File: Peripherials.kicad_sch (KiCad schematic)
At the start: 24 parts, among them J10 IDC_Cable_02x08, J6 Conn_01x02_Pin, J7 USB_C_Receptacle_USB2.0_14P, J8 USB_C_Receptacle_USB2.0_14P, Q1 NMOS, U5 USBLC6-2P6, U6 USBLC6-2P6

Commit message: Major Changes - Schematic Done??
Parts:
- added C41: 100n, Capacitor_SMD:C_0603_1608Metric, symbol Device:C
- added J18: Micro_SD_Card, Connector_Card:microSD_HC_Hirose_DM3BT-DSF-PEJS, symbol Connector:Micro_SD_Card
- added R61, R62: DNP, Resistor_SMD:R_0603_1608Metric, symbol Device:R
- C22: renamed from C26; footprint (none) -> Capacitor_SMD:C_0603_1608Metric
- C23: renamed from C27; footprint (none) -> Capacitor_SMD:C_0603_1608Metric
- C24: renamed from C25; footprint (none) -> Capacitor_SMD:C_0603_1608Metric
- C25: renamed from C28; footprint (none) -> Capacitor_SMD:C_0603_1608Metric
- D6: renamed from D2; footprint Package_TO_SOT_SMD:SOT-666 -> Diode_SMD:D_1206_3216Metric_Pad1.42x1.75mm_HandSolder
- D7: renamed from D1; footprint Package_TO_SOT_SMD:SOT-666 -> Diode_SMD:D_1206_3216Metric_Pad1.42x1.75mm_HandSolder
- D8: renamed from D3; footprint Package_TO_SOT_SMD:SOT-666 -> Diode_SMD:D_0805_2012Metric_Pad1.15x1.40mm_HandSolder
- J12: renamed from J7; footprint (none) -> Connector_USB:USB_C_Receptacle_Palconn_UTC16-G
- J13: renamed from J8; footprint (none) -> Connector_USB:USB_C_Receptacle_Palconn_UTC16-G
- J15: renamed from J6; footprint (none) -> Connector_PinHeader_2.54mm:PinHeader_1x02_P2.54mm_Vertical
- Q2: renamed from Q1; footprint (none) -> Package_TO_SOT_SMD:SOT-23
- R44: renamed from R10; footprint Package_DIP:DIP-8_W7.62mm -> Resistor_SMD:R_0603_1608Metric
- R45: renamed from R14; footprint Package_DIP:DIP-8_W7.62mm -> Resistor_SMD:R_0603_1608Metric
- R46: renamed from R11; footprint Package_DIP:DIP-8_W7.62mm -> Resistor_SMD:R_0603_1608Metric
- R47: renamed from R15; footprint Package_DIP:DIP-8_W7.62mm -> Resistor_SMD:R_0603_1608Metric
- R48: renamed from R13; footprint Package_DIP:DIP-8_W7.62mm -> Resistor_SMD:R_0603_1608Metric
- R49: renamed from R12; footprint Package_DIP:DIP-8_W7.62mm -> Resistor_SMD:R_0603_1608Metric
- R50: renamed from R17; footprint Package_DIP:DIP-8_W7.62mm -> Resistor_SMD:R_0603_1608Metric
- R51: renamed from R16; footprint Package_DIP:DIP-8_W7.62mm -> Resistor_SMD:R_0603_1608Metric
- R52: renamed from R24; footprint Package_DIP:DIP-8_W7.62mm -> Resistor_SMD:R_0603_1608Metric
- R53: renamed from R23; footprint Package_DIP:DIP-8_W7.62mm -> Resistor_SMD:R_0603_1608Metric
- renumbered J10 to J14, U5 to U12, U6 to U13
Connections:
- net GND: now also C41.2, J18.6 (VSS), J18.SH (SHIELD), R61.1, R62.1
- net at J13.SH (SHIELD): now also R62.2
- net at J12.SH (SHIELD): now also R61.2
- net +5V renamed 5V
- net USB_D_N_ESD renamed USB_P_ESP_ESD
- net USB_P_ESP_ESD: no longer R49.2, U12.3 (I/O2)
- net USB_D_N_Resistor renamed USB_N_ESP_RES
- net USB_N_ESP_RES: no longer J12.A7 (D-), J12.B7 (D-), R48.1
- net USB_D_P_ESD renamed USB_N_ESP_ESD
- net USB_N_ESP_ESD: no longer R48.2, U12.1 (I/O1)
- net USB_D_P_Resistor renamed USB_P_ESP_RES
- net USB_P_ESP_RES: no longer J12.A6 (D+), J12.B6 (D+), R49.1
- new net 3V3: C41.1, J18.4 (VDD)
- new net SPI1_MISO: J18.7 (DAT0)
- new net SPI1_MOSI: J18.8 (DAT1)
- new net SPI1_SCLK: J18.5 (CLK)
- new net SPI_CS_SD_CARD: J18.3 (CMD)
- new net USB_N_STM_ESD: R48.2, U12.1 (I/O1)
- new net USB_N_STM_RES: J12.A7 (D-), J12.B7 (D-), R48.1
- new net USB_P_STM_ESD: R49.2, U12.3 (I/O2)
- new net USB_P_STM_RES: J12.A6 (D+), J12.B6 (D+), R49.1
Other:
- note added: "MICRO SD CARD"
- note removed: "IR EMITTER"
- moved on the sheet: C22, C23, C24, C25, D6, D7, D8, J12, J13, J14, J15, Q2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

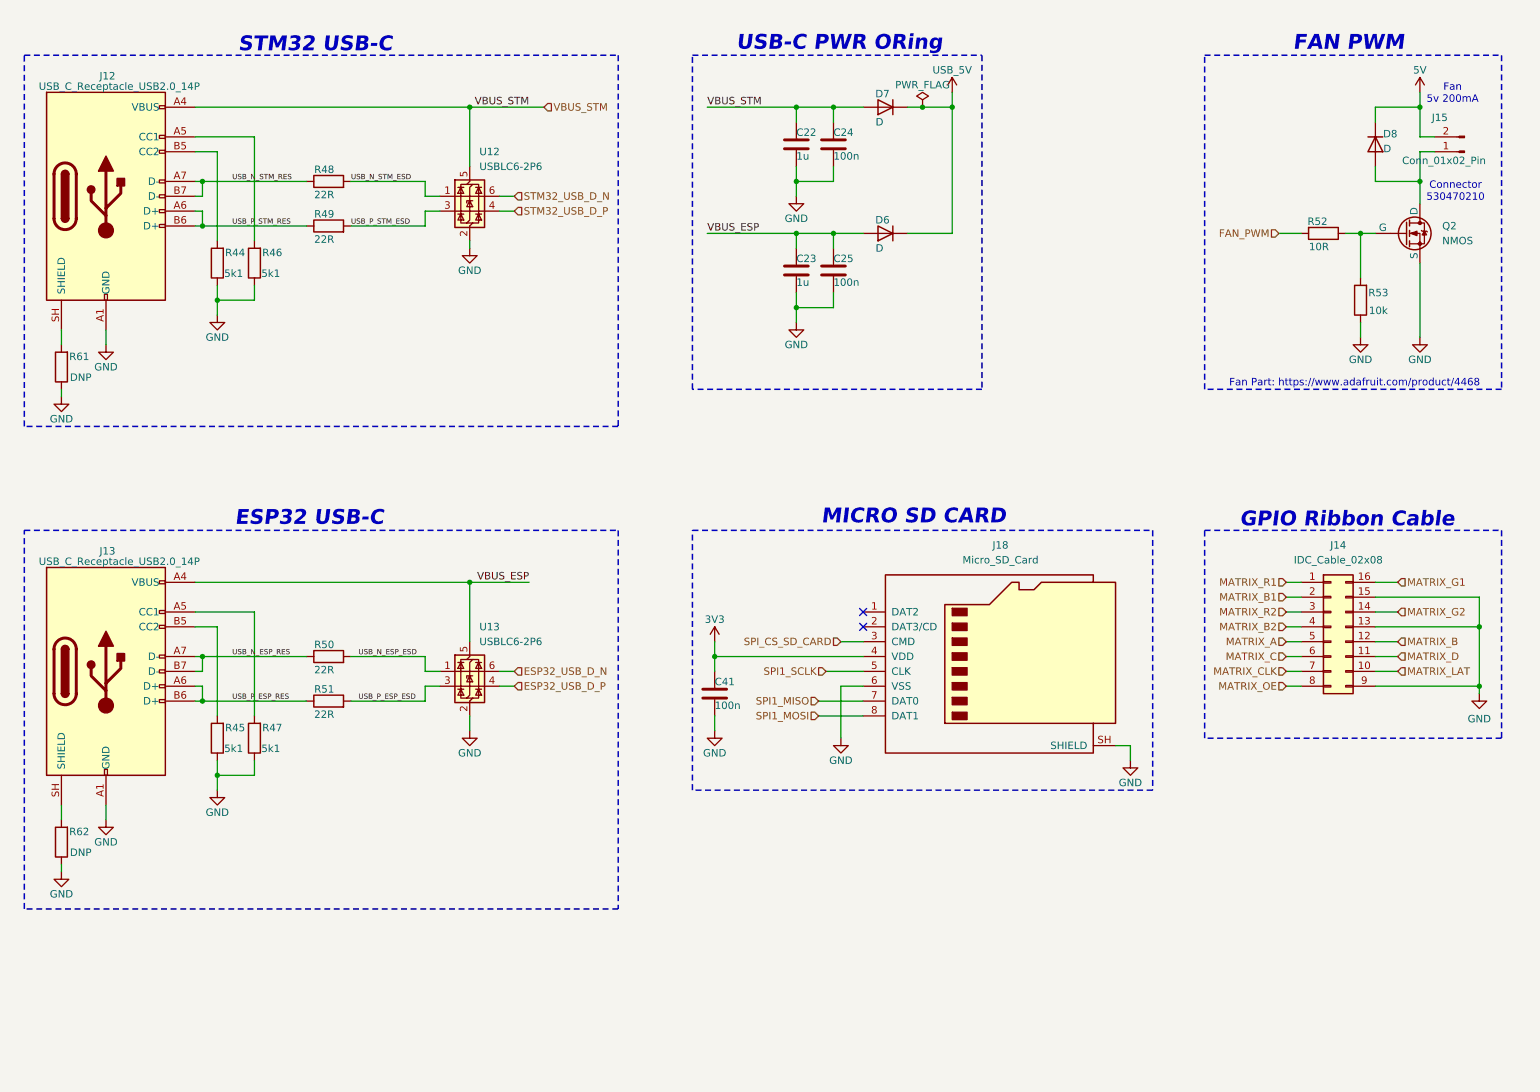
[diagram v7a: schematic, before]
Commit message: PCB Start, Schematic polish
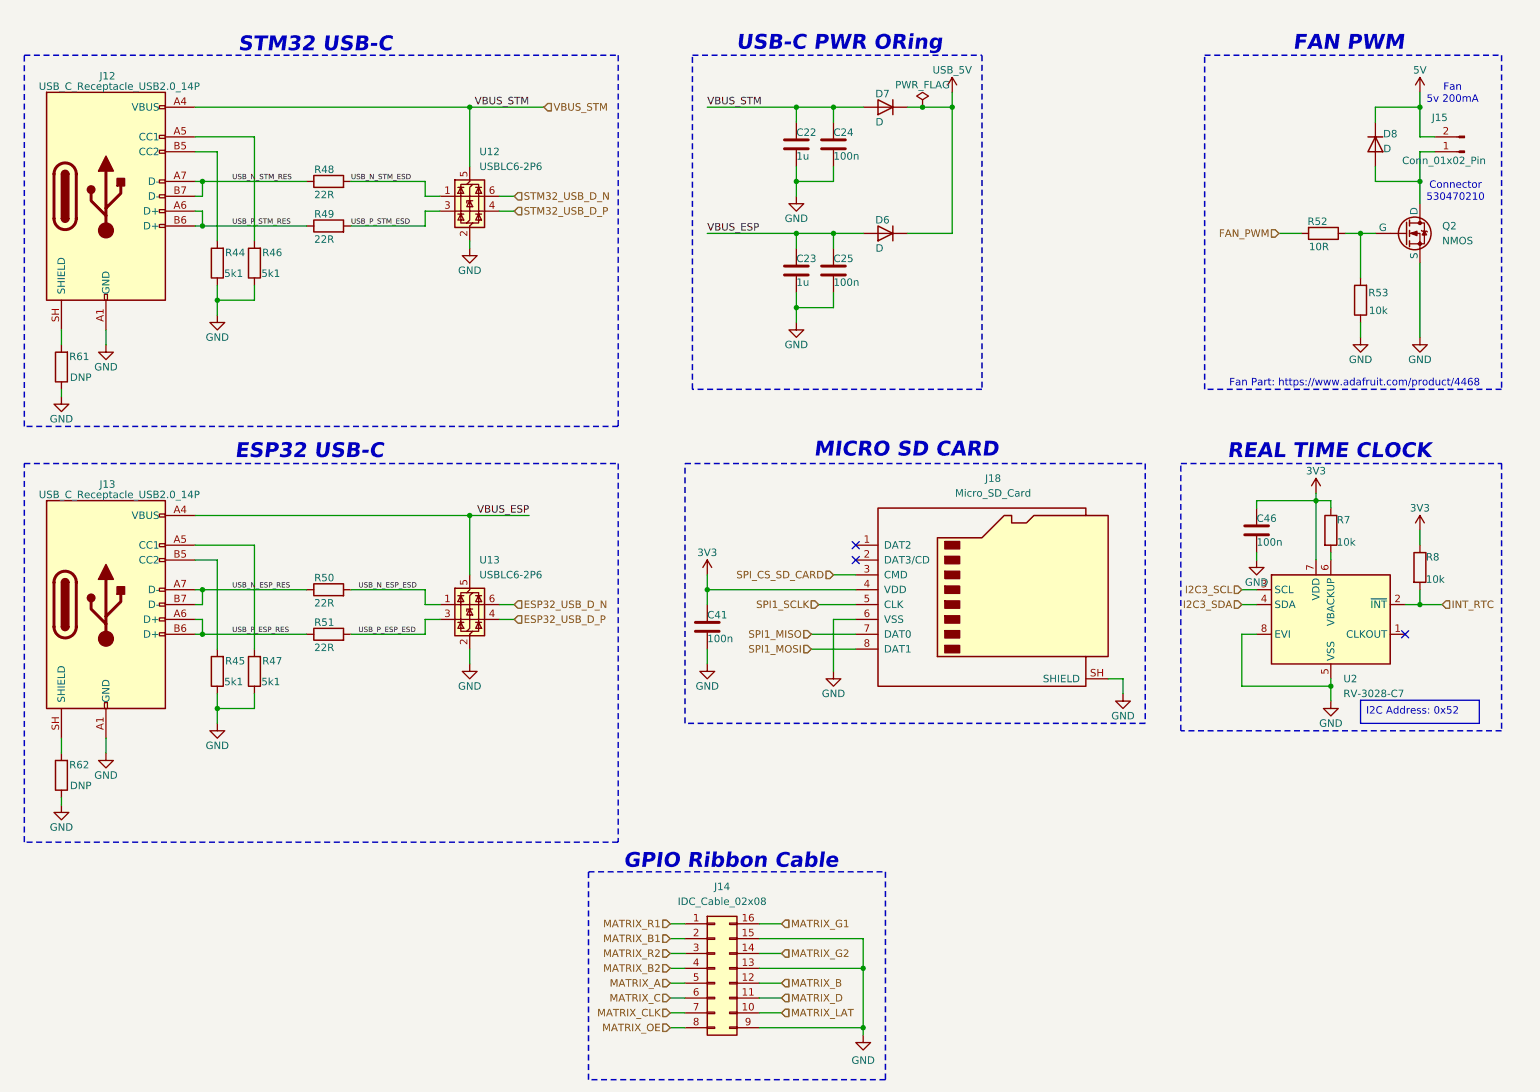
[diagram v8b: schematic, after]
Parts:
- added C46: 100n, Capacitor_SMD:C_0603_1608Metric, symbol Device:C
- added R7, R8: 10k, Resistor_SMD:R_0603_1608Metric, symbol Device:R
- added U2: RV-3028-C7, Package_SON:MicroCrystal_C7_SON-8_1.5x3.2mm_P0.9mm, symbol Timer_RTC:RV-3028-C7
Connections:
- net 3V3: now also C46.1, R7.1, R8.1, U2.7 (VDD)
- net GND: now also C46.2, U2.5 (VSS), U2.8 (EVI)
- new net: R7.2, U2.6 (VBACKUP)
- new net I2C3_SCL: U2.3 (SCL)
- new net I2C3_SDA: U2.4 (SDA)
- new net INT_RTC: R8.2, U2.2 (~{INT})
- no-connect marks 2 -> 3
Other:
- note added: "REAL TIME CLOCK"
- moved on the sheet: C41, J13, J14, J18, R45, R47, R50, R51, R62, U13
